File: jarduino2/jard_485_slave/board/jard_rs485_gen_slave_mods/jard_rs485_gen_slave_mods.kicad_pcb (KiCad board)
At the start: 2 copper layers, 94 x 94 mm, 58 parts, among them J1 NETWORK IN, J10 Conn_01x02, J2 NETWORK OUT, J3 Conn_01x03, J4 LED, J5 Conn_01x02, J6 Conn_01x03, J7 Conn_01x03, J8 Conn_01x02, J9 Conn_01x02, Q1 2N2222A, Q2 2N2222A, Q3 bpc_mos_p03p4, Q4 bpc_mos_p03p4, U1 BPC_Mod485, U2 MCP6002-xP

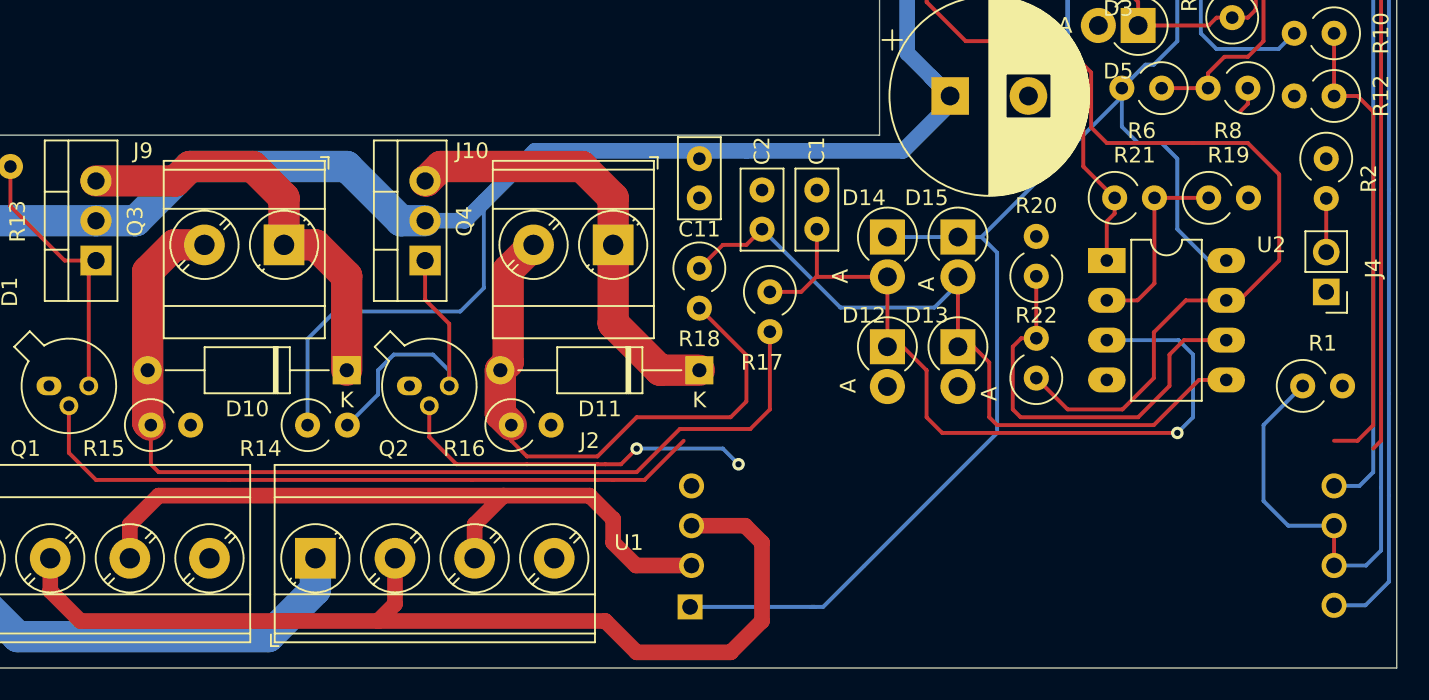
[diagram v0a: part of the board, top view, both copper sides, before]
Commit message: Agrandir sérigraphie connecteurs bus Correction erreur inversion sérigraphie 1 et 4 sur J2 Correction inversion RX/TX sur module RS485 Inversion sérigraphie Niveaux/Débit
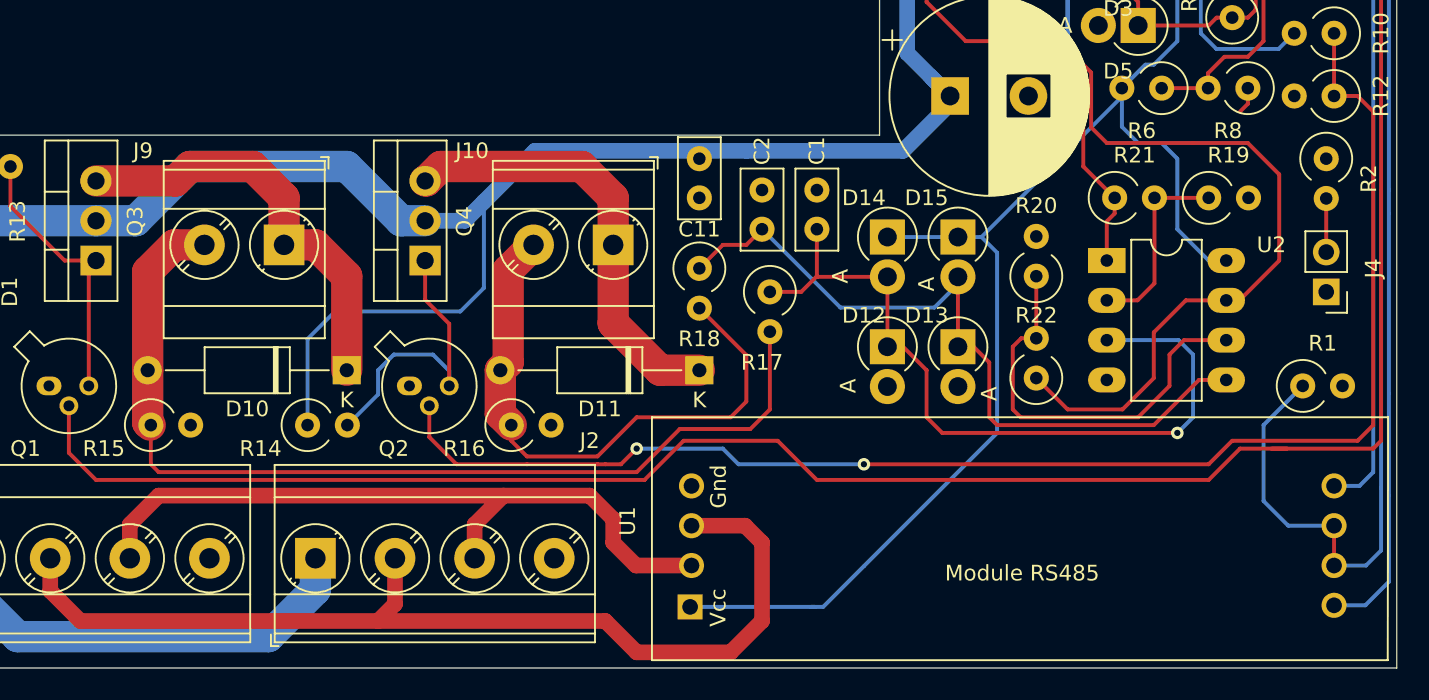
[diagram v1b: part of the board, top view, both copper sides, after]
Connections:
- U1 pad 5: RX -> TX
- U1 pad 8: TX -> RX
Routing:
- net Net-(Q1-Pad2): track 80.8 -> 127.7 mm
- net Net-(Q2-Pad2): track 53.1 -> 91.7 mm
